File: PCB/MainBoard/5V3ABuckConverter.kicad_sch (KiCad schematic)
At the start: 13 parts, among them U1 TPS56339DDC

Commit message: passed ERC in schematic
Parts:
- C10, C11, C12, C13, C14, C15: footprint (none) -> Capacitor_SMD:C_1206_3216Metric_Pad1.33x1.80mm_HandSolder
- JP2: footprint (none) -> Jumper:SolderJumper-2_P1.3mm_Open_TrianglePad1.0x1.5mm
- L2: footprint (none) -> Inductor_SMD:L_1206_3216Metric
- R6, R7: footprint (none) -> Resistor_THT:R_Axial_DIN0207_L6.3mm_D2.5mm_P7.62mm_Horizontal
- TP3, TP4: footprint (none) -> Connector_PinHeader_2.54mm:PinHeader_1x01_P2.54mm_Vertical
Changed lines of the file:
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@@
 		)
 	)
-	(hierarchical_label "12V_IN"
+	(hierarchical_label "+12V"
 		(shape input)
 		(at 74.93 91.44 180)
@@
 		)
 	)
-	(hierarchical_label "5V_3A"
-		(shape input)
+	(hierarchical_label "+5V_3A"
+		(shape output)
 		(at 214.63 91.44 0)
 		(fields_autoplaced yes)
@@
 			)
 		)
-		(property "Footprint" ""
+		(property "Footprint" "Capacitor_SMD:C_1206_3216Metric_Pad1.33x1.80mm_HandSolder"
 			(at 160.9852 99.06 0)
 			(effects
@@
 				(path "/ce4aa5cc-bc13-46ce-a61c-95c4be48f850/7cb6be40-ad14-404d-82c5-ced68dcd093c/4fef1ee3-4720-43a9-aff6-10e8deab9b92"
 					(reference "C14")
-					(unit 1)
-				)
-			)
-		)
-	)
-	(symbol
-		(lib_id "power:+5V")
-		(at 209.55 78.74 0)
-		(unit 1)
-		(exclude_from_sim no)
-		(in_bom yes)
-		(on_board yes)
-		(dnp no)
-		(fields_autoplaced yes)
-		(property "Reference" "#PWR045"
-			(at 209.55 82.55 0)
-			(effects
-				(font
-					(size 1.27 1.27)
-				)
-				(hide yes)
-			)
-		)
-		(property "Value" "+5V_3A"
-			(at 209.55 73.66 0)
-			(effects
-				(font
-					(size 1.27 1.27)
-				)
-			)
-		)
-		(property "Footprint" ""
-			(at 209.55 78.74 0)
-			(effects
-				(font
-					(size 1.27 1.27)
-				)
-				(hide yes)
-			)
-		)
-		(property "Datasheet" ""
-			(at 209.55 78.74 0)
-			(effects
-				(font
-					(size 1.27 1.27)
-				)
-				(hide yes)
-			)
-		)
-		(property "Description" ""
-			(at 209.55 78.74 0)
-			(effects
-				(font
-					(size 1.27 1.27)
-				)
-				(hide yes)
-			)
-		)
-		(pin "1"
-		)
-		(instances
-			(project "MainBoard"
-				(path "/ce4aa5cc-bc13-46ce-a61c-95c4be48f850/7cb6be40-ad14-404d-82c5-ced68dcd093c/4fef1ee3-4720-43a9-aff6-10e8deab9b92"
-					(reference "#PWR045")
 					(unit 1)
 				)
@@
 			)
 		)
-		(property "Footprint" ""
+		(property "Footprint" "Capacitor_SMD:C_1206_3216Metric_Pad1.33x1.80mm_HandSolder"
 			(at 103.8352 100.33 0)
 			(effects
@@
 			)
 		)
-		(property "Footprint" ""
+		(property "Footprint" "Resistor_THT:R_Axial_DIN0207_L6.3mm_D2.5mm_P7.62mm_Horizontal"
 			(at 181.102 95.25 90)
 			(effects
@@
 			)
 		)
-		(property "Footprint" ""
+		(property "Footprint" "Capacitor_SMD:C_1206_3216Metric_Pad1.33x1.80mm_HandSolder"
 			(at 139.3952 91.44 0)
 			(effects
@@
 			)
 		)
-		(property "Footprint" ""
+		(property "Footprint" "Connector_PinHeader_2.54mm:PinHeader_1x01_P2.54mm_Vertical"
 			(at 187.96 76.2 0)
 			(effects
@@
 			)
 		)
-		(property "Footprint" ""
+		(property "Footprint" "Jumper:SolderJumper-2_P1.3mm_Open_TrianglePad1.0x1.5mm"
 			(at 194.31 91.44 0)
 			(effects
@@
 			)
 		)
-		(property "Footprint" ""
+		(property "Footprint" "Capacitor_SMD:C_1206_3216Metric_Pad1.33x1.80mm_HandSolder"
 			(at 83.5152 100.33 0)
 			(effects
@@
 				(path "/ce4aa5cc-bc13-46ce-a61c-95c4be48f850/7cb6be40-ad14-404d-82c5-ced68dcd093c/4fef1ee3-4720-43a9-aff6-10e8deab9b92"
 					(reference "C10")
+					(unit 1)
+				)
+			)
+		)
+	)
+	(symbol
+		(lib_id "power:+5V")
+		(at 209.55 78.74 0)
+		(unit 1)
+		(exclude_from_sim no)
+		(in_bom yes)
+		(on_board yes)
+		(dnp no)
+		(fields_autoplaced yes)
+		(property "Reference" "#PWR045"
+			(at 209.55 82.55 0)
+			(effects
+				(font
+					(size 1.27 1.27)
+				)
+				(hide yes)
+			)
+		)
+		(property "Value" "+5V_3A"
+			(at 209.55 73.66 0)
+			(effects
+				(font
+					(size 1.27 1.27)
+				)
+			)
+		)
+		(property "Footprint" ""
+			(at 209.55 78.74 0)
+			(effects
+				(font
+					(size 1.27 1.27)
+				)
+				(hide yes)
+			)
+		)
+		(property "Datasheet" ""
+			(at 209.55 78.74 0)
+			(effects
+				(font
+					(size 1.27 1.27)
+				)
+				(hide yes)
+			)
+		)
+		(property "Description" "Power symbol creates a global label with name \"+5V\""
+			(at 209.55 78.74 0)
+			(effects
+				(font
+					(size 1.27 1.27)
+				)
+				(hide yes)
+			)
+		)
+		(pin "1"
+		)
+		(instances
+			(project "MainBoard"
+				(path "/ce4aa5cc-bc13-46ce-a61c-95c4be48f850/7cb6be40-ad14-404d-82c5-ced68dcd093c/4fef1ee3-4720-43a9-aff6-10e8deab9b92"
+					(reference "#PWR045")
 					(unit 1)
 				)
@@
 			)
 		)
-		(property "Footprint" ""
+		(property "Footprint" "Capacitor_SMD:C_1206_3216Metric_Pad1.33x1.80mm_HandSolder"
 			(at 172.4152 99.06 0)
 			(effects
@@
 			)
 		)
-		(property "Footprint" ""
+		(property "Footprint" "Inductor_SMD:L_1206_3216Metric"
 			(at 153.67 91.44 0)
 			(effects
@@
 			)
 		)
-		(property "Footprint" ""
+		(property "Footprint" "Capacitor_SMD:C_1206_3216Metric_Pad1.33x1.80mm_HandSolder"
 			(at 93.6752 100.33 0)
 			(effects
@@
 			)
 		)
-		(property "Footprint" ""
+		(property "Footprint" "Resistor_THT:R_Axial_DIN0207_L6.3mm_D2.5mm_P7.62mm_Horizontal"
 			(at 181.102 107.95 90)
 			(effects
@@
 			)
 		)
-		(property "Footprint" ""
+		(property "Footprint" "Connector_PinHeader_2.54mm:PinHeader_1x01_P2.54mm_Vertical"
 			(at 185.42 119.38 0)
 			(effects

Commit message: Placed Buck Converters and changed inductors to 1008
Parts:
- L2: footprint Inductor_SMD:L_1206_3216Metric -> Inductor_SMD:L_1008_2520Metric
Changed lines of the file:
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@@
 			)
 		)
-		(property "Footprint" "Inductor_SMD:L_1206_3216Metric"
+		(property "Footprint" "Inductor_SMD:L_1008_2520Metric"
 			(at 153.67 91.44 0)
 			(effects

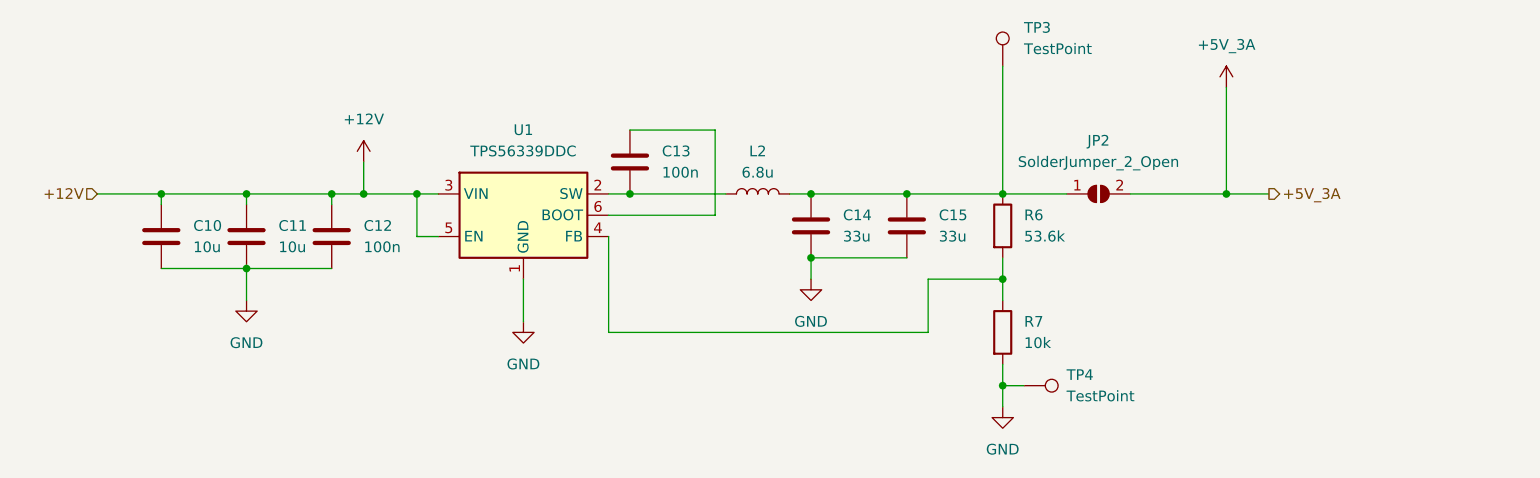
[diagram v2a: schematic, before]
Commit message: updating PCB with new components and proper footprints, still need to fix footprint matching issue.
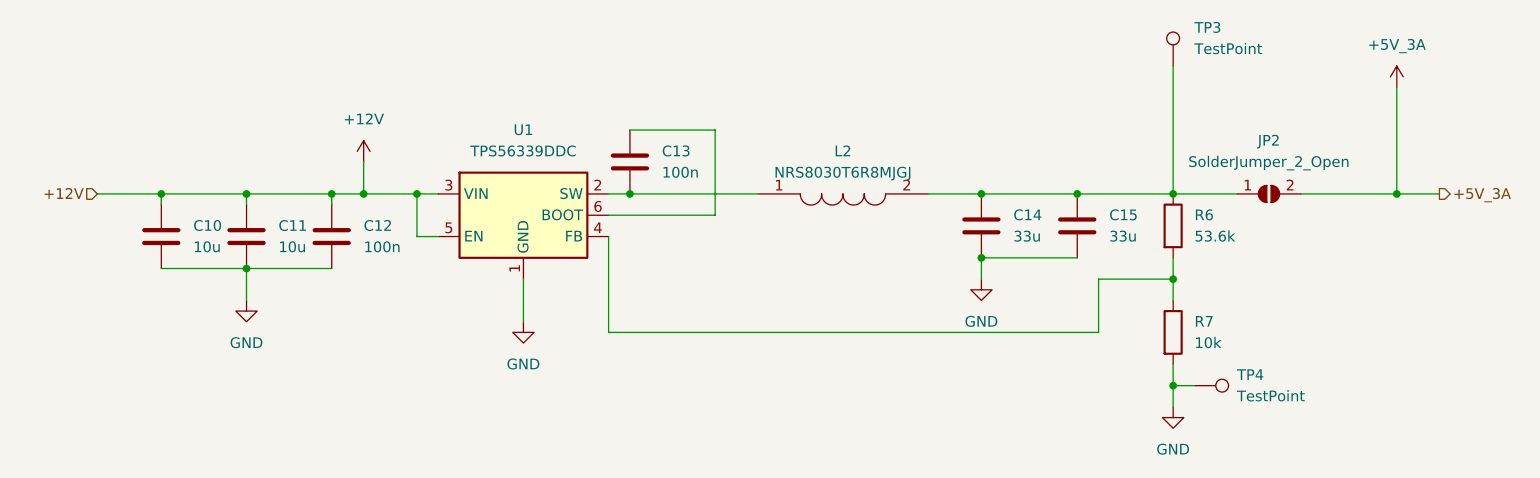
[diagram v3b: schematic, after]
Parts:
- removed L2: 6.8u, Inductor_SMD:L_1008_2520Metric, symbol Device:L
- added L2: NRS8030T6R8MJGJ, ProjectLibrary:NRS8030T6R8MJGJ, symbol CustomSymbols:NRS8030T6R8MJGJ
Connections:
- net at C14.1, C15.1, JP2.1 (A)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: now also L2.2
- net at C13.2, U1.2 (SW): now also L2.1
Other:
- moved on the sheet: C14, C15, JP2, R6, R7, TP3, TP4
